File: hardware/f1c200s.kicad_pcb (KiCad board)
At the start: 4 copper layers, 60 x 56 mm, 46 parts, among them J1 Micro_SD_Card, J10 Conn_01x07, J11 Conn_02x05_Odd_Even, J12 Conn_02x03_Odd_Even, J2 USB_B_Micro, J3 Conn_01x03, J4 Conn_01x07, J5 Jumper, J6 Jumper, J7 Jumper, J8 Jumper, J9 Conn_01x01, Q1 2N7002, SW1 SW_Push, U1 F1C100s, U2 LDK130PU-R, U3 LDK130PU-R, U4 LDK130PU-R, Y1 XRCGB24M000F0G00R0

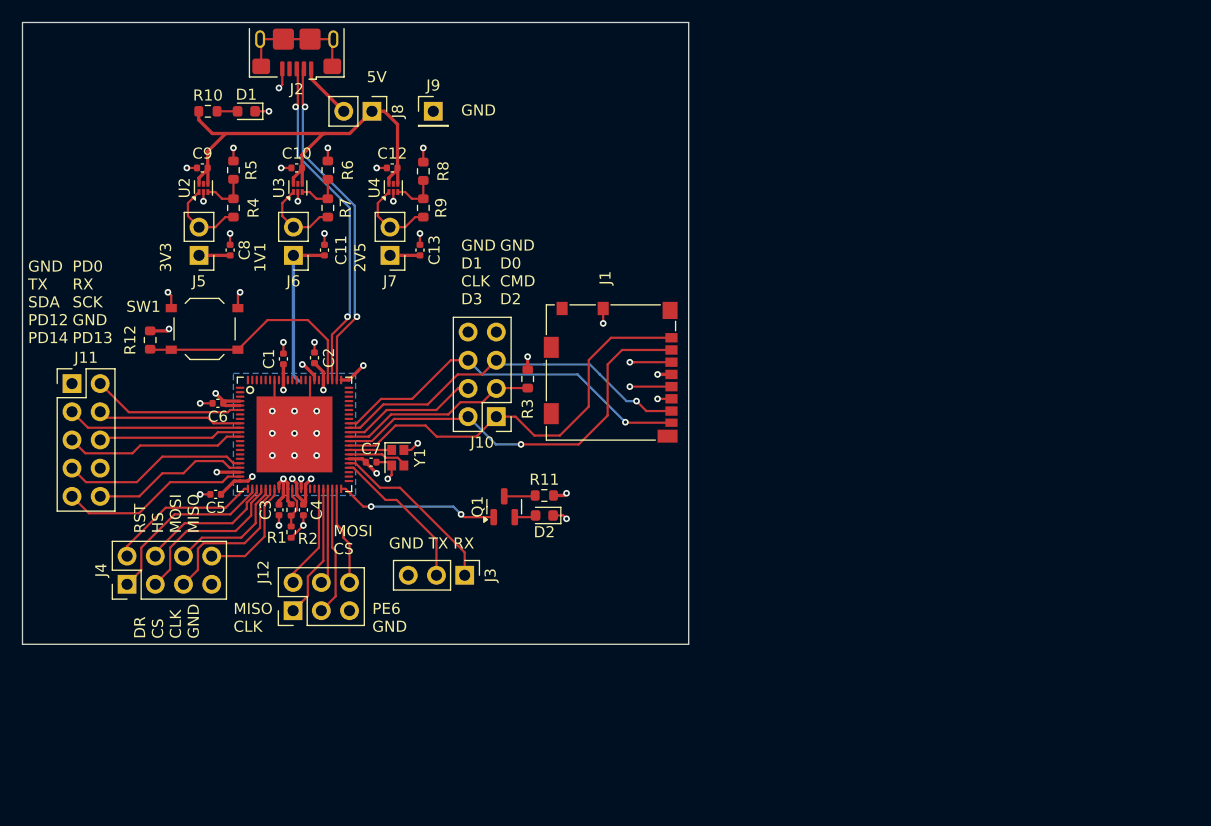
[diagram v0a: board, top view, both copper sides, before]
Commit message: Adding ESP32 to board, work in progress
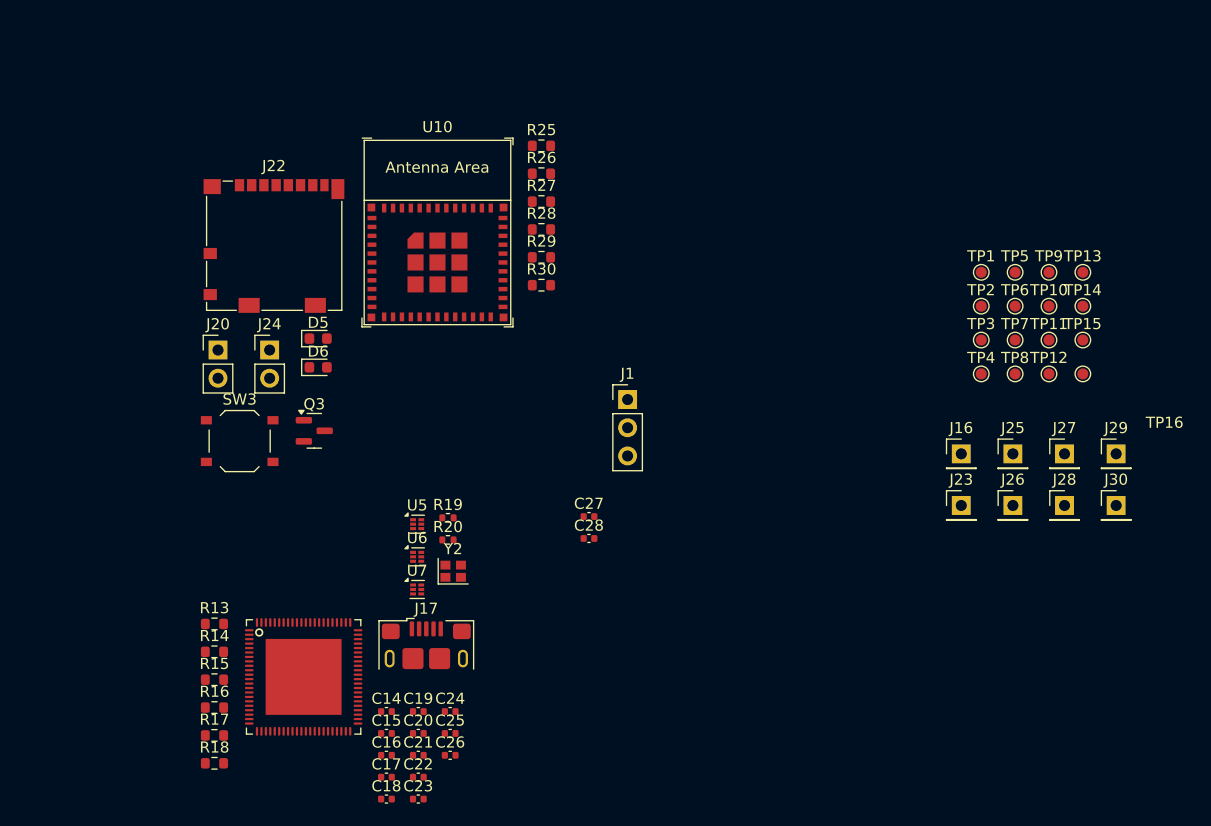
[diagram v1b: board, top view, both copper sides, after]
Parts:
- removed C1, C3, C5, C6: 10uF, Capacitor_SMD:C_0402_1005Metric
- removed C10, C11, C12, C13, C2, C4, C7, C8, C9: 1uF, Capacitor_SMD:C_0402_1005Metric
- removed D1, D2: Yellow, LED_SMD:LED_0603_1608Metric
- removed J10, J4: Conn_01x07, Connector_PinHeader_2.54mm:PinHeader_2x04_P2.54mm_Vertical
- removed J11: Conn_02x05_Odd_Even, Connector_PinHeader_2.54mm:PinHeader_2x05_P2.54mm_Vertical
- removed J12: Conn_02x03_Odd_Even, Connector_PinHeader_2.54mm:PinHeader_2x03_P2.54mm_Vertical
- removed J2: USB_B_Micro, Connector_USB:USB_Micro-B_Amphenol_10118193-0001LF_Horizontal
- removed J3: Conn_01x03, Connector_PinHeader_2.54mm:PinHeader_1x03_P2.54mm_Vertical
- removed J5, J6, J7, J8: Jumper, Connector_PinHeader_2.54mm:PinHeader_1x02_P2.54mm_Vertical
- removed J9: Conn_01x01, Connector_PinHeader_2.54mm:PinHeader_1x01_P2.54mm_Vertical
- removed Q1: 2N7002, Package_TO_SOT_SMD:SOT-23
- removed R1, R2: 4.7k, Resistor_SMD:R_0402_1005Metric
- removed R10, R11: 510, Resistor_SMD:R_0603_1608Metric
- removed R12, R3: 10K, Resistor_SMD:R_0603_1608Metric
- removed R4, R6: 5.6k, Resistor_SMD:R_0603_1608Metric
- removed R5: 1.8k, Resistor_SMD:R_0603_1608Metric
- removed R7: 2.2k, Resistor_SMD:R_0603_1608Metric
- removed R8: 3.6k, Resistor_SMD:R_0603_1608Metric
- removed R9: 8.2k, Resistor_SMD:R_0603_1608Metric
- removed SW1: SW_Push, Button_Switch_SMD:SW_Push_1P1T_XKB_TS-1187A
- removed U2, U3, U4: LDK130PU-R, Package_DFN_QFN:DFN-6_1.3x1.2mm_P0.4mm
- removed Y1: XRCGB24M000F0G00R0, Crystal:Crystal_SMD_2016-4Pin_2.0x1.6mm
- added C14: 1uF, Capacitor_SMD:C_0402_1005Metric, F.Cu at (158.3, 125.1)
- added C15: 1uF, Capacitor_SMD:C_0402_1005Metric, F.Cu at (158.3, 127.0)
- added C16: 1uF, Capacitor_SMD:C_0402_1005Metric, F.Cu at (158.3, 129.0)
- added C17: 1uF, Capacitor_SMD:C_0402_1005Metric, F.Cu at (158.3, 131.0)
- added C18: 1uF, Capacitor_SMD:C_0402_1005Metric, F.Cu at (158.3, 132.9)
- added C19: 1uF, Capacitor_SMD:C_0402_1005Metric, F.Cu at (161.2, 125.1)
- added C20: 10uF, Capacitor_SMD:C_0402_1005Metric, F.Cu at (161.2, 127.0)
- added C21: 1uF, Capacitor_SMD:C_0402_1005Metric, F.Cu at (161.2, 129.0)
- added C22: 10uF, Capacitor_SMD:C_0402_1005Metric, F.Cu at (161.2, 131.0)
- added C23: 10uF, Capacitor_SMD:C_0402_1005Metric, F.Cu at (161.2, 132.9)
- added C24: 1uF, Capacitor_SMD:C_0402_1005Metric, F.Cu at (164.0, 125.1)
- added C25: 10uF, Capacitor_SMD:C_0402_1005Metric, F.Cu at (164.0, 127.0)
- added C26: 1uF, Capacitor_SMD:C_0402_1005Metric, F.Cu at (164.0, 129.0)
- added C27: 1uF, Capacitor_SMD:C_0402_1005Metric, F.Cu at (176.5, 107.5)
- added C28: 10uF, Capacitor_SMD:C_0402_1005Metric, F.Cu at (176.5, 109.5)
- added D5: Yellow, LED_SMD:LED_0603_1608Metric, F.Cu at (152.1, 91.5)
- added D6: Yellow, LED_SMD:LED_0603_1608Metric, F.Cu at (152.1, 94.1)
- added J16: Conn_01x01, Connector_PinHeader_2.54mm:PinHeader_1x01_P2.54mm_Vertical, F.Cu at (210.1, 101.8)
- added J17: USB_B_Micro, Connector_USB:USB_Micro-B_Amphenol_10118193-0001LF_Horizontal, F.Cu at (161.9, 120.3)
- added J20: Jumper, Connector_PinHeader_2.54mm:PinHeader_1x02_P2.54mm_Vertical, F.Cu at (143.1, 92.5)
- added J22: Micro_SD_Card, Connector_Card:microSD_HC_Molex_104031-0811, F.Cu at (148.2, 83.1)
- added J23: Conn_01x01, Connector_PinHeader_2.54mm:PinHeader_1x01_P2.54mm_Vertical, F.Cu at (210.1, 106.5)
- added J24: Jumper, Connector_PinHeader_2.54mm:PinHeader_1x02_P2.54mm_Vertical, F.Cu at (147.8, 92.5)
- added J25: Conn_01x01, Connector_PinHeader_2.54mm:PinHeader_1x01_P2.54mm_Vertical, F.Cu at (214.7, 101.8)
- added J26: Conn_01x01, Connector_PinHeader_2.54mm:PinHeader_1x01_P2.54mm_Vertical, F.Cu at (214.7, 106.5)
- added J27: Conn_01x01, Connector_PinHeader_2.54mm:PinHeader_1x01_P2.54mm_Vertical, F.Cu at (219.3, 101.8)
- added J28: Conn_01x01, Connector_PinHeader_2.54mm:PinHeader_1x01_P2.54mm_Vertical, F.Cu at (219.3, 106.5)
- added J29: Conn_01x01, Connector_PinHeader_2.54mm:PinHeader_1x01_P2.54mm_Vertical, F.Cu at (224.0, 101.8)
- added J30: Conn_01x01, Connector_PinHeader_2.54mm:PinHeader_1x01_P2.54mm_Vertical, F.Cu at (224.0, 106.5)
- added Q3: 2N7002, Package_TO_SOT_SMD:SOT-23, F.Cu at (151.8, 99.8)
- added R13: 5.6k, Resistor_SMD:R_0603_1608Metric, F.Cu at (142.8, 117.2)
- added R14: 1.8k, Resistor_SMD:R_0603_1608Metric, F.Cu at (142.8, 119.7)
- added R15: 2.2k, Resistor_SMD:R_0603_1608Metric, F.Cu at (142.8, 122.2)
- added R16: 5.6k, Resistor_SMD:R_0603_1608Metric, F.Cu at (142.8, 124.7)
- added R17: 8.2k, Resistor_SMD:R_0603_1608Metric, F.Cu at (142.8, 127.2)
- added R18: 3.6k, Resistor_SMD:R_0603_1608Metric, F.Cu at (142.8, 129.7)
- added R19: 4.7k, Resistor_SMD:R_0402_1005Metric, F.Cu at (163.8, 107.6)
- added R20: 4.7k, Resistor_SMD:R_0402_1005Metric, F.Cu at (163.8, 109.6)
- added R25: 10K, Resistor_SMD:R_0603_1608Metric, F.Cu at (172.2, 74.1)
- added R26: 10K, Resistor_SMD:R_0603_1608Metric, F.Cu at (172.2, 76.6)
- added R27: 10K, Resistor_SMD:R_0603_1608Metric, F.Cu at (172.2, 79.1)
- added R28: 10K, Resistor_SMD:R_0603_1608Metric, F.Cu at (172.2, 81.6)
- added R29: 510, Resistor_SMD:R_0603_1608Metric, F.Cu at (172.2, 84.2)
- added R30: 510, Resistor_SMD:R_0603_1608Metric, F.Cu at (172.2, 86.7)
- added SW3: SW_Push, Button_Switch_SMD:SW_Push_1P1T_XKB_TS-1187A, F.Cu at (145.1, 100.7)
- added TP1: TestPoint_Small, TestPoint:TestPoint_Pad_D1.0mm, F.Cu at (211.8, 85.5)
- added TP10: TestPoint_Small, TestPoint:TestPoint_Pad_D1.0mm, F.Cu at (217.9, 88.5)
- added TP11: TestPoint_Small, TestPoint:TestPoint_Pad_D1.0mm, F.Cu at (217.9, 91.6)
- added TP12: TestPoint_Small, TestPoint:TestPoint_Pad_D1.0mm, F.Cu at (217.9, 94.7)
- added TP13: TestPoint_Small, TestPoint:TestPoint_Pad_D1.0mm, F.Cu at (221.0, 85.5)
- added TP14: TestPoint_Small, TestPoint:TestPoint_Pad_D1.0mm, F.Cu at (221.0, 88.5)
- added TP15: TestPoint_Small, TestPoint:TestPoint_Pad_D1.0mm, F.Cu at (221.0, 91.6)
- added TP16: TestPoint_Small, TestPoint:TestPoint_Pad_D1.0mm, F.Cu at (221.0, 94.7)
- added TP2: TestPoint_Small, TestPoint:TestPoint_Pad_D1.0mm, F.Cu at (211.8, 88.5)
- added TP3: TestPoint_Small, TestPoint:TestPoint_Pad_D1.0mm, F.Cu at (211.8, 91.6)
- added TP4: TestPoint_Small, TestPoint:TestPoint_Pad_D1.0mm, F.Cu at (211.8, 94.7)
- added TP5: TestPoint_Small, TestPoint:TestPoint_Pad_D1.0mm, F.Cu at (214.9, 85.5)
- added TP6: TestPoint_Small, TestPoint:TestPoint_Pad_D1.0mm, F.Cu at (214.9, 88.5)
- added TP7: TestPoint_Small, TestPoint:TestPoint_Pad_D1.0mm, F.Cu at (214.9, 91.6)
- added TP8: TestPoint_Small, TestPoint:TestPoint_Pad_D1.0mm, F.Cu at (214.9, 94.7)
- added TP9: TestPoint_Small, TestPoint:TestPoint_Pad_D1.0mm, F.Cu at (217.9, 85.5)
- added U10: ESP32-C3-MINI-1, PCM_Espressif:ESP32-C3-MINI-1, F.Cu at (162.9, 81.9)
- added U5: LDK130PU-R, Package_DFN_QFN:DFN-6_1.3x1.2mm_P0.4mm, F.Cu at (161.0, 108.2)
- added U6: LDK130PU-R, Package_DFN_QFN:DFN-6_1.3x1.2mm_P0.4mm, F.Cu at (161.0, 111.1)
- added U7: LDK130PU-R, Package_DFN_QFN:DFN-6_1.3x1.2mm_P0.4mm, F.Cu at (161.0, 114.1)
- added Y2: XRCGB24M000F0G00R0, Crystal:Crystal_SMD_2016-4Pin_2.0x1.6mm, F.Cu at (164.3, 112.4)
- J1: value Micro_SD_Card -> Conn_01x03; footprint Connector_Card:microSD_HC_Molex_104031-0811 -> Connector_PinHeader_2.54mm:PinHeader_1x03_P2.54mm_Vertical
- moved U1 21.9 mm to (150.8, 121.9)
- moved J1 2.88 mm to (180.0, 97.0), turned to 0 degrees
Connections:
- J1 pad 1: /SDC0_D2 -> UART0_RX
- J1 pad 2: /SDC0_D3 -> UART0_TX
- J1 pad 3: /SDC0_CMD -> GND
- U1 pad 10: /UART1_TX -> ESP_TX
- U1 pad 11: /I2C1_SCK -> unconnected-(U1A-PD5/LCD_D7/TWI1_SCK/EINTD5-Pad11)
- U1 pad 12: /I2C1_SDA -> unconnected-(U1A-PD6/LCD_D10/TWI1_SDA/EINTD6-Pad12)
- U1 pad 13: /DA_MCLK -> unconnected-(U1A-PD7/LCD_D11/DA_MCLK/EINTD7-Pad13)
- U1 pad 14: /DA_BCLK -> unconnected-(U1A-PD8/LCD_D12/DA_BCLK/EINTD8-Pad14)
- U1 pad 15: /DA_LRCK -> unconnected-(U1A-PD9/LCD_D13/DA_LRCK/EINTD9-Pad15)
- U1 pad 16: /DA_IN -> unconnected-(U1A-PD10/LCD_D14/DA_IN/EINTD10-Pad16)
- U1 pad 17: /DA_OUT -> unconnected-(U1A-PD11/LCD_D15/DA_OUT/EINTD11-Pad17)
- U1 pad 18: /PD12 -> unconnected-(U1A-PD12/LCD_D18/TWI0_SCK/RSB_SCK/EINTD12-Pad18)
- U1 pad 19: /PD13 -> unconnected-(U1A-PD13/LCD_D19/UART2_TX/EINTD13-Pad19)
- U1 pad 21: /PD14 -> unconnected-(U1A-PD14/LCD_D20/UART2_RX/EINTD14-Pad21)
- U1 pad 23: /ESP_RST -> ESP_RST
- U1 pad 24: /ESP_DR -> ESP_DR
- U1 pad 25: /ESP_HS -> ESP_HS
- U1 pad 26: /SPI0_CS -> ESP_CS
- U1 pad 27: /SPI0_MOSI -> ESP_MOSI
- U1 pad 28: /SPI0_CLK -> ESP_CLK
- U1 pad 29: /SPI0_MISO -> ESP_MISO
- U1 pad 37: /I2C0_SDA -> unconnected-(U1A-PE12/DA_MCLK/TWI0_SDA/PWM0/EINTE12-Pad37)
- U1 pad 38: /I2C0_SCK -> unconnected-(U1A-PE11/CLK_OUT/TWI0_SCK/IR_RX/EINTE11-Pad38)
- U1 pad 39: /SPI1_MISO -> unconnected-(U1A-PE10/CSI_D7/UART2_CTS/SPI1_MISO/EINTE10-Pad39)
- U1 pad 40: /SPI1_CLK -> unconnected-(U1A-PE9/CSI_D6/UART2_RTS/SPI1_CLK/EINTE9-Pad40)
- U1 pad 41: /SPI1_MOSI -> unconnected-(U1A-PE8/CSI_D5/UART2_RX/SPI1_MOSI/EINTE8-Pad41)
- U1 pad 42: /SPI1_CS -> unconnected-(U1A-PE7/CSI_D4/UART2_TX/SPI1_CS/EINTE7-Pad42)
- U1 pad 43: /PE6 -> unconnected-(U1A-PE6/CSI_D3/PWM1/DA_OUT/OWA_OUT/EINTE6-Pad43)
- U1 pad 44: /Heartbeat -> unconnected-(U1A-PE5/CSI_D2/LCD_D17/DA_IN/EINTE5-Pad44)
- U1 pad 45: /PE4 -> unconnected-(U1A-PE4/CSI_D1/LCD_D16/DA_LRCK/RSB_SDA/EINTE4-Pad45)
- U1 pad 46: /PE3 -> unconnected-(U1A-PE3/CSI_D0/LCD_D9/DA_BCLK/RSB_SCK/EINTE3-Pad46)
- U1 pad 47: /PE2 -> unconnected-(U1A-PE2/CSI_PCLK/LCD_D8/CLK_OUT/EINTE2-Pad47)
- U1 pad 48: /UART0_TX -> UART0_TX
- U1 pad 49: /UART0_RX -> UART0_RX
- U1 pad 51: /HOSCI -> /cpu/HOSCI
- U1 pad 52: /HOSCO -> /cpu/HOSCO
- U1 pad 53: /SDC0_D2 -> SDC0_D2
- U1 pad 54: /SDC0_D3 -> SDC0_D3
- U1 pad 55: /SDC0_CMD -> SDC0_CMD
- U1 pad 56: /SDC0_CLK -> SDC0_CLK
- U1 pad 57: /SDC0_D0 -> SDC0_D0
- U1 pad 58: /SDC0_D1 -> SDC0_D1
- U1 pad 59: /SCD1_CLK -> unconnected-(U1A-PC0/SPI0_CLK/SDC1_CLK-Pad59)
- U1 pad 6: /PD0 -> unconnected-(U1A-PD0/LCD_D2/TWI0_SDA/RSB_SDA/EINTD0-Pad6)
- U1 pad 60: /SDC1_CMD -> unconnected-(U1A-PC1/SPI0_CS/SDC1_CMD-Pad60)
- U1 pad 61: /SDC1_D0 -> unconnected-(U1A-PC2/SPI0_MISO/SDC1_D0-Pad61)
- U1 pad 62: /PC3 -> unconnected-(U1A-PC3/SPI0_MOSI/UART0_TX-Pad62)
- U1 pad 68: /D- -> /cpu/D-
- U1 pad 69: /D+ -> /cpu/D+
- U1 pad 7: /UART1_RTS -> unconnected-(U1A-PD1/LCD_D3/UART1_RTS/EINTD1-Pad7)
- U1 pad 70: /~{RST} -> ~{RST}
- U1 pad 79: /LRADC0 -> unconnected-(U1A-LRADC0-Pad79)
- U1 pad 8: /UART1_CTS -> ESP_BOOT
- U1 pad 9: /UART1_RX -> ESP_RX
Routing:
- net GND: track 56.6 -> 0.00 mm, vias 36 -> 0
- net +5V: track 41.9 -> 0.00 mm
- net /SDC0_D2: track 37.8 -> 0.00 mm
- net /SDC0_D3: track 37.2 -> 0.00 mm, vias 1 -> 0
- net /SDC0_CMD: track 34.7 -> 0.00 mm, vias 1 -> 0
- net /SDC0_D1: track 33.7 -> 0.00 mm, vias 1 -> 0
- net /SDC0_D0: track 33.5 -> 0.00 mm, vias 1 -> 0
- net /SDC0_CLK: track 31.8 -> 0.00 mm, vias 1 -> 0
- net /D-: track 31.0 -> 0.00 mm, vias 2 -> 0
- net /D+: track 30.8 -> 0.00 mm, vias 2 -> 0
- net +2V5: track 30.3 -> 0.00 mm, vias 4 -> 0
- net +3V3: track 22.2 -> 0.00 mm, vias 9 -> 0
- net /~{RST}: track 21.5 -> 0.00 mm
- net +1V1: track 21.5 -> 0.00 mm, vias 3 -> 0
- net /PD14: track 17.1 -> 0.00 mm
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- removed copper zone on B.Cu, net +1V1
- removed copper zone on In2.Cu, net +2V5
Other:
- board outline removed
- board text removed: "1V1"
- board text removed: "2V5"
- board text removed: "3V3"
- board text removed: "5V"
- board text removed: "DR CS CLK GND"
- board text removed: "GND"
- board text removed: "GND D0 CMD D2"
- board text removed: "GND D1 CLK D3"
- board text removed: "GND TX RX"
- board text removed: "GND TX SDA PD12 PD14"
- board text removed: "MISO CLK"
- board text removed: "MOSI CS"
- board text removed: "PD0 RX SCK GND PD13"
- board text removed: "PE6 GND"
- board text removed: "RST HS MOSI MISO"
